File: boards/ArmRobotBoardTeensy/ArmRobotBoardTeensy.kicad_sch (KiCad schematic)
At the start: 49 parts, among them U1 Teensy4.0

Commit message: Prepare for manufacturing
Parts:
- renumbered 555C1 to C1, 555C2 to C2, RPWM1ALED1 to D1, PWM2SLED1 to D10, PWM3SLED1 to D11, LPWM1ALED1 to D2, RPWM2ALED1 to D3, LPWM2ALED1 to D4, PWM1SLED1 to D5, RPWM3ALED1 to D6, LPWM3ALED1 to D7, SPILED1 to D8, SOLED1 to D9, SPI1 to J1, PWM3 to J10, SOL1 to J11, QUAD1 to J2, ADC2 to J3, ADC1 to J4, I2C1 to J5, LIM2 to J6, LIM1 to J7, PWM1 to J8, PWM2 to J9, PWM1ENT1 to Q1, RPWM1ALEDR1 to R1, SPILEDR1 to R10, SOLEDR1 to R11, PWM2SLEDR1 to R12, PWM3SLEDR1 to R13, PWM1ENTR1 to R14, 555RA1 to R15, 555RB1 to R16, LPWM1ALEDR1 to R2, RPWM2ALEDR1 to R3, LPWM2ALEDR1 to R4, PWM1SLEDR1 to R5, RPWM3ALEDR1 to R6, LPWM3ALEDR1 to R7, PWM1LIMR1 to R8, PWM1ENR1 to R9, 555TIMER1 to U2, GATE1 to U3, GATE2 to U4
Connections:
- net A0: now also J3.2 (Pin_2); no longer J4.2 (Pin_2)
- net A1: now also J4.2 (Pin_2); no longer J3.2 (Pin_2)
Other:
- moved on the sheet: J1, J10, J11, J2, J3, J4, J5, J8, J9

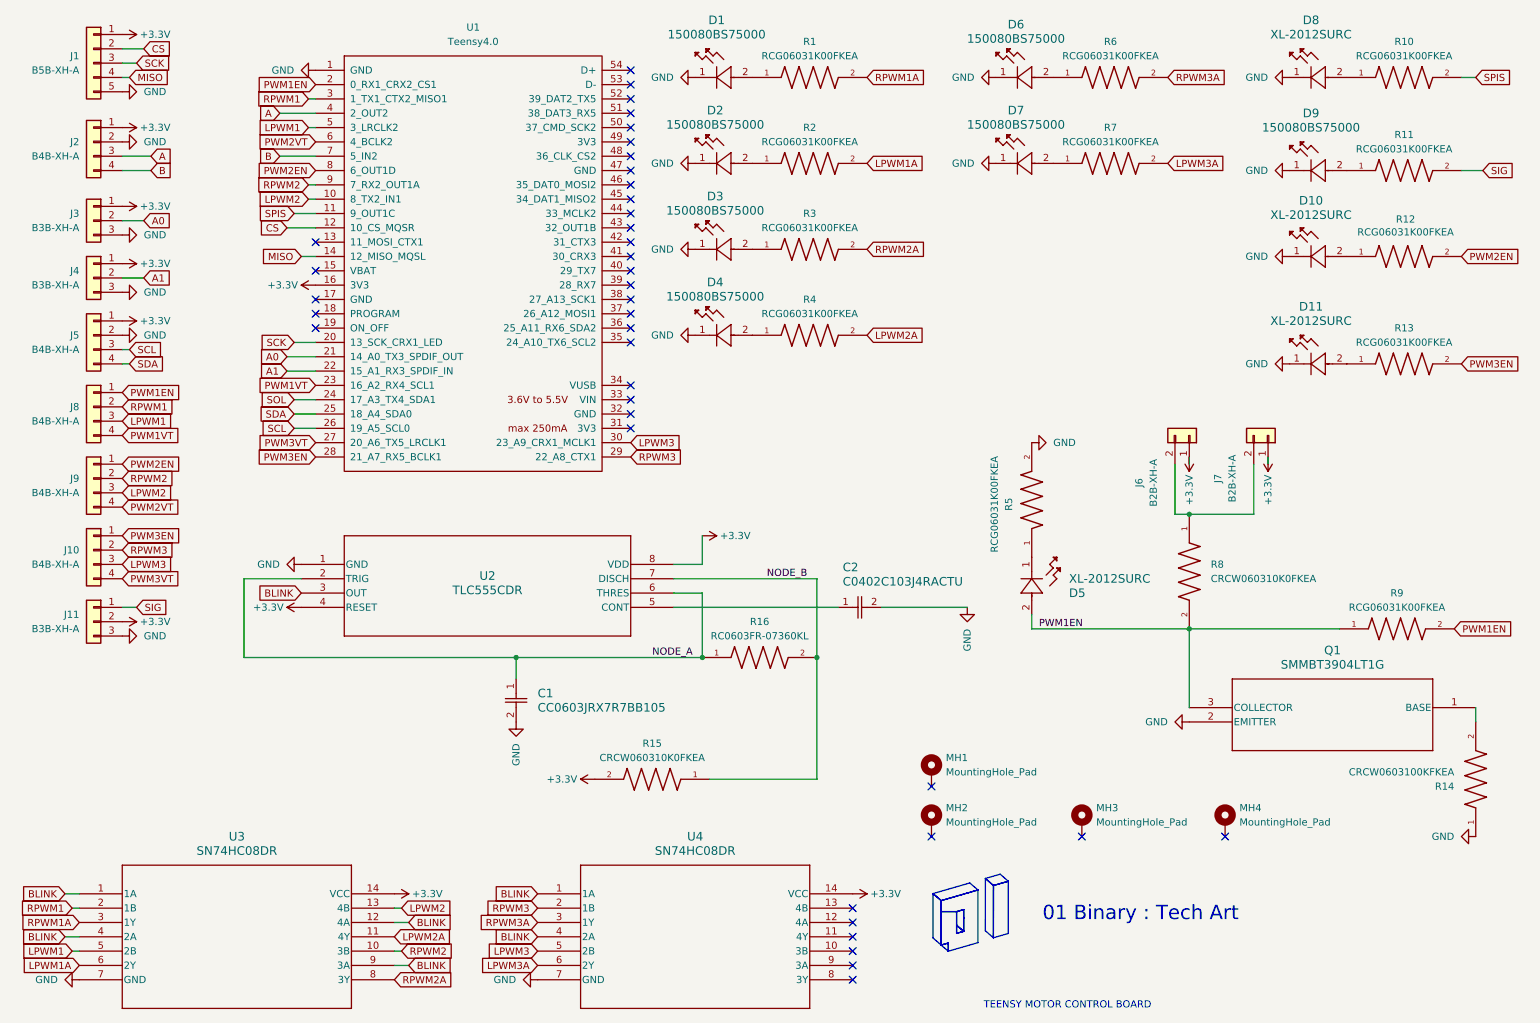
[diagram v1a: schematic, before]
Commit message: Address ERC and DRC violations
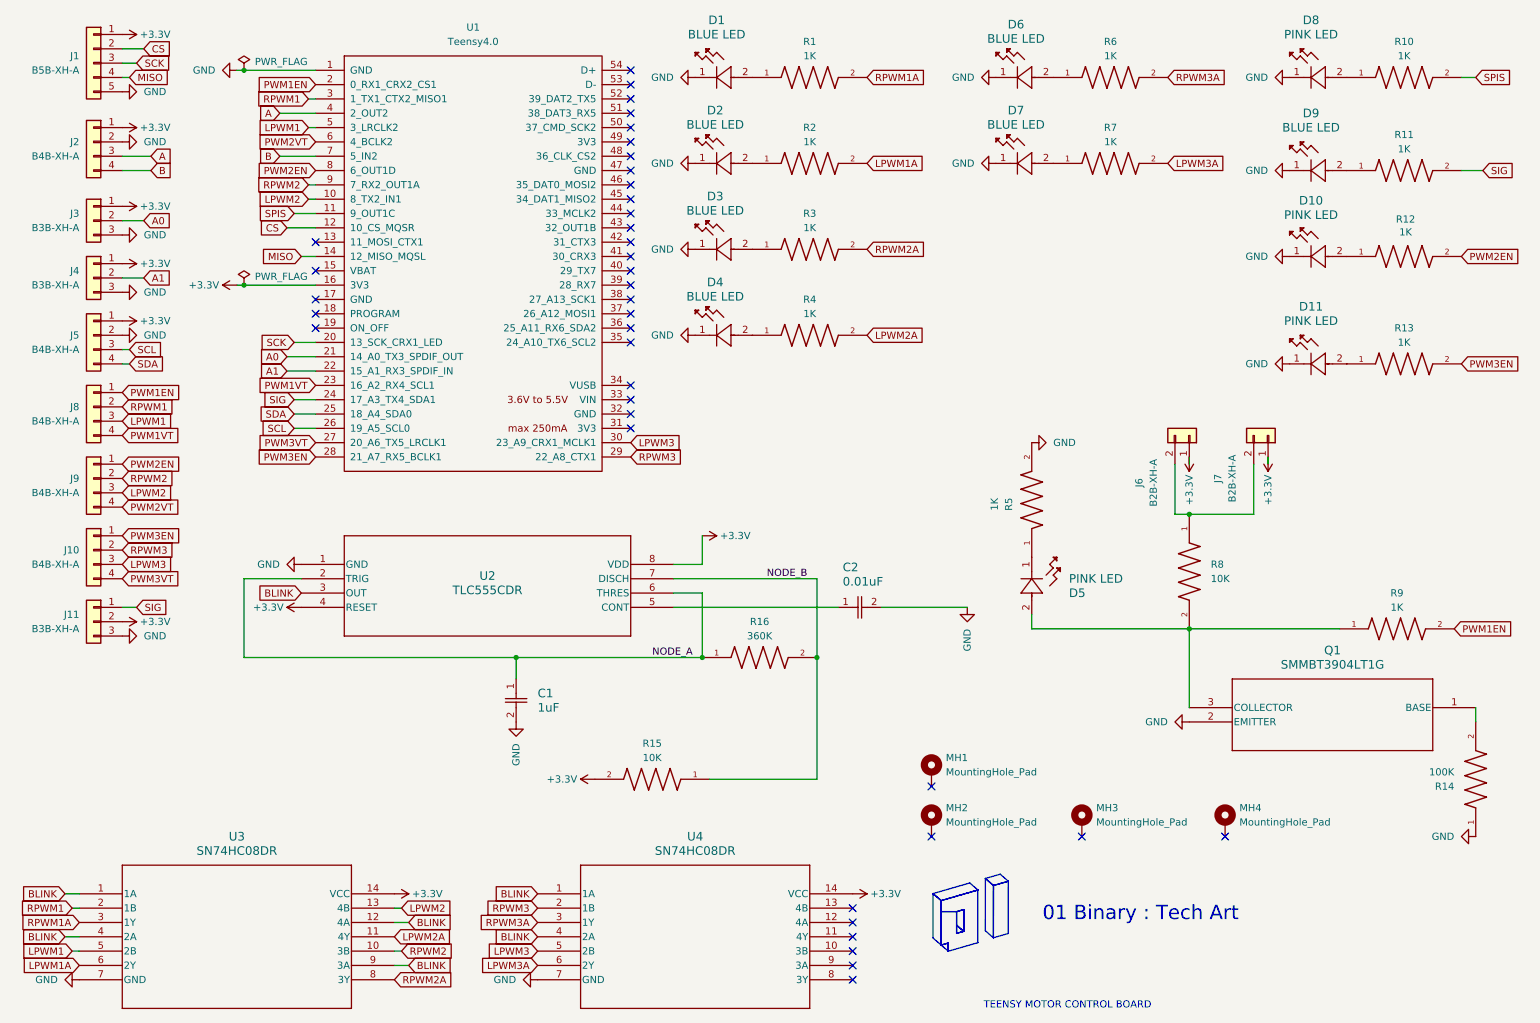
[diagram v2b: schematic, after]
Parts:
- C1: value CC0603JRX7R7BB105 -> 1uF
- C2: value C0402C103J4RACTU -> 0.01uF
- D1, D2, D3, D4, D6, D7, D9: value 150080BS75000 -> BLUE LED
- D10, D11, D5, D8: value XL-2012SURC -> PINK LED
- R1, R10, R11, R12, R13, R2, R3, R4, R5, R6, R7, R9: value RCG06031K00FKEA -> 1K
- R14: value CRCW0603100KFKEA -> 100K
- R15, R8: value CRCW060310K0FKEA -> 10K
- R16: value RC0603FR-07360KL -> 360K
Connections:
- net SOL is gone; now on net SIG: U1.24 (17_A3_TX4_SDA1)
- net PWM1EN: no longer D5.2, Q1.3 (COLLECTOR), R8.2, R9.1
- new net: D5.2, Q1.3 (COLLECTOR), R8.2, R9.1

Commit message: Fixed LED footprint and re-exported
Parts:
- D1, D2, D3, D4, D6, D7, D9: footprint 150080BS75000:150080BS75000 -> 150080BS75000:150080BS75000_Modified
- D10, D11, D5, D8: footprint LED_XL-2012:LED_XL-2012SURC_XLG -> XL-2012UPC:LED_XL-2012SURC_XLG
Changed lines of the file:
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@@
 			)
 		)
-		(property "Footprint" "LED_XL-2012:LED_XL-2012SURC_XLG"
+		(property "Footprint" "XL-2012UPC:LED_XL-2012SURC_XLG"
 			(at 252.73 76.2 0)
 			(effects
@@
 			)
 		)
-		(property "Footprint" "150080BS75000:150080BS75000"
+		(property "Footprint" "150080BS75000:150080BS75000_Modified"
 			(at 147.32 25.4 0)
 			(effects
@@
 			)
 		)
-		(property "Footprint" "150080BS75000:150080BS75000"
+		(property "Footprint" "150080BS75000:150080BS75000_Modified"
 			(at 252.73 41.91 0)
 			(effects
@@
 			)
 		)
-		(property "Footprint" "150080BS75000:150080BS75000"
+		(property "Footprint" "150080BS75000:150080BS75000_Modified"
 			(at 147.32 40.64 0)
 			(effects
@@
 			)
 		)
-		(property "Footprint" "150080BS75000:150080BS75000"
+		(property "Footprint" "150080BS75000:150080BS75000_Modified"
 			(at 200.66 40.64 0)
 			(effects
@@
 			)
 		)
-		(property "Footprint" "150080BS75000:150080BS75000"
+		(property "Footprint" "150080BS75000:150080BS75000_Modified"
 			(at 200.66 25.4 0)
 			(effects
@@
 			)
 		)
-		(property "Footprint" "150080BS75000:150080BS75000"
+		(property "Footprint" "150080BS75000:150080BS75000_Modified"
 			(at 147.32 55.88 0)
 			(effects
@@
 			)
 		)
-		(property "Footprint" "150080BS75000:150080BS75000"
+		(property "Footprint" "150080BS75000:150080BS75000_Modified"
 			(at 147.32 71.12 0)
 			(effects
@@
 			)
 		)
-		(property "Footprint" "LED_XL-2012:LED_XL-2012SURC_XLG"
+		(property "Footprint" "XL-2012UPC:LED_XL-2012SURC_XLG"
 			(at 196.85 120.65 0)
 			(effects
@@
 			)
 		)
-		(property "Footprint" "LED_XL-2012:LED_XL-2012SURC_XLG"
+		(property "Footprint" "XL-2012UPC:LED_XL-2012SURC_XLG"
 			(at 252.73 25.4 0)
 			(effects
@@
 			)
 		)
-		(property "Footprint" "LED_XL-2012:LED_XL-2012SURC_XLG"
+		(property "Footprint" "XL-2012UPC:LED_XL-2012SURC_XLG"
 			(at 252.73 57.15 0)
 			(effects
